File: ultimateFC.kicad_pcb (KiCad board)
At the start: 6 copper layers, 36 x 36 mm, 247 parts, among them J1 Conn_Coaxial, J2 Conn_Coaxial, J3 Conn_Coaxial, J4 Conn_Coaxial, J5 Conn_Coaxial, J6 Conn_Coaxial, J7 USB_B_Micro, SW1 SW_Push, U1 LMR33630CQRNX, U2 TPS62824ADMQ, U3 LMR33620CRNXT, U4 S25FL064L, U5 DPS310, U6 STM32H735VGH6, U7 ICM-20602, U8 BMI270, Y1 CSTNE8M00G550000R0

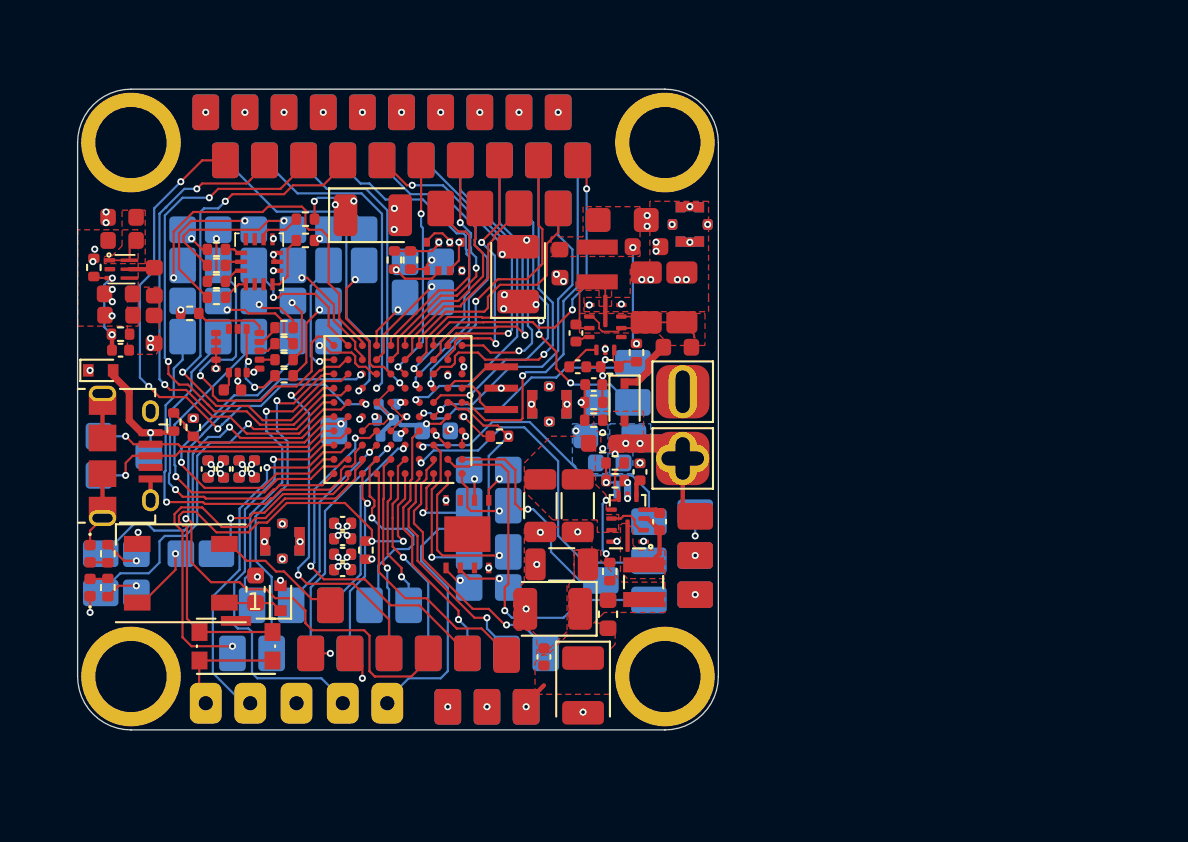
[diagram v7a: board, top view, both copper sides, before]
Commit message: tons of vias
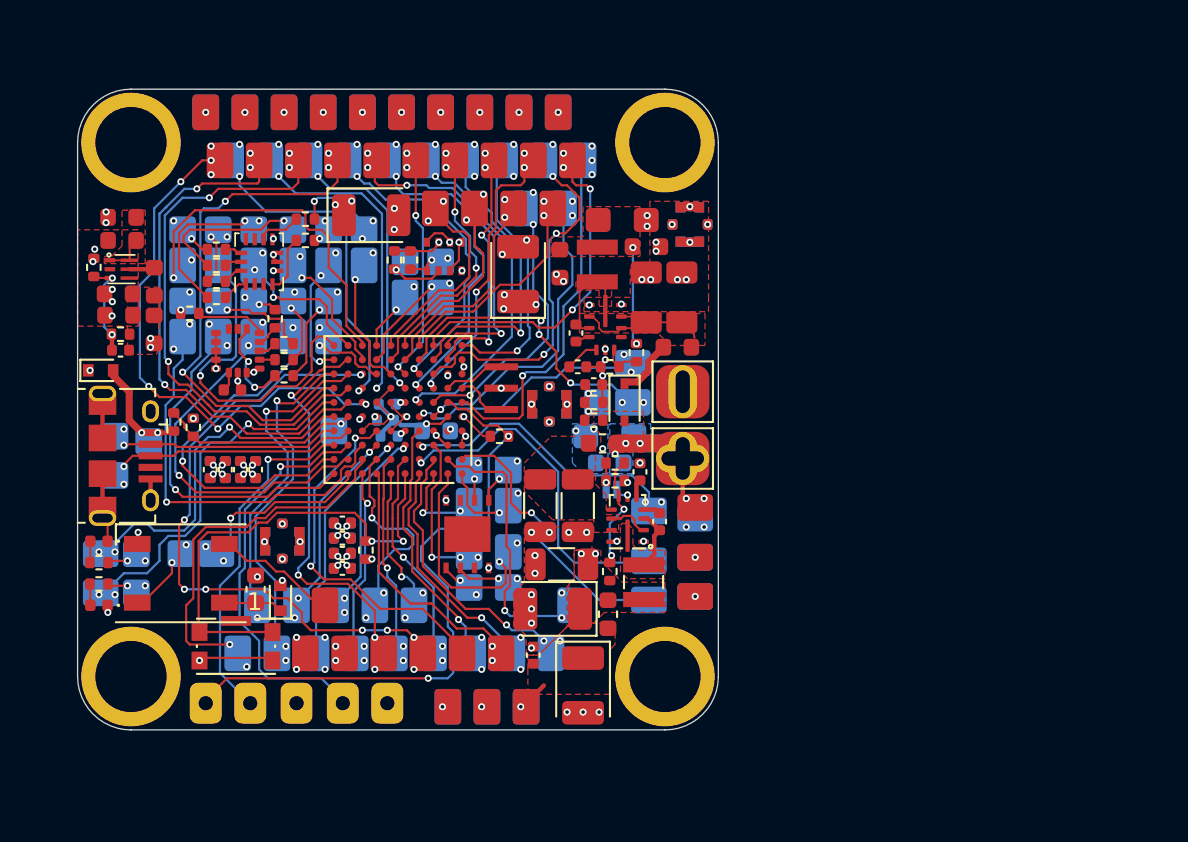
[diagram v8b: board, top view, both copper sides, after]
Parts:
- moved TP25 10.2 mm to (114.4, 131.5)
- moved TP88 10.2 mm to (104.2, 131.5)
- moved TP110 5.20 mm to (106.7, 131.5)
- moved TP111 5.20 mm to (111.9, 131.5)
- moved TP124 4.41 mm to (124.7, 126.0), turned to 180 degrees
- moved TP107 2.92 mm to (129.1, 125.7)
- moved D5 1.12 mm to (98.2, 126.0), turned to 180 degrees
- moved TP136 0.90 mm to (99.1, 116.5)
- moved TP137 0.90 mm to (99.1, 118.7)
- moved D4 0.86 mm to (98.2, 122.4), turned to 180 degrees
- moved TP138 0.80 mm to (101.0, 116.8)
- moved R14 0.71 mm to (108.1, 109.9), turned to -90 degrees
- moved R25 0.71 mm to (98.2, 123.6), turned to 180 degrees
- moved C39 0.61 mm to (122.6, 128.8)
- moved TP114 0.60 mm to (129.1, 120.7)
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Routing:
- net /NRST: track 25.4 -> 36.5 mm, vias 1 -> 2
- net Net-(TP124-Pad1): track 20.3 -> 14.8 mm, vias 1 -> 3
- net Net-(R12-Pad1): track 30.4 -> 26.4 mm
- net SWDIO: track 23.0 -> 19.6 mm
- net +3V3: track 20.3 -> 16.9 mm, vias 24 -> 26
- net MISO_FLASH: track 8.17 -> 11.4 mm, vias 1 -> 2
- net Net-(TP73-Pad1): track 23.3 -> 20.2 mm, vias 1 -> 2
- net Net-(TP107-Pad1): track 12.5 -> 15.6 mm
- net SWDCLK: track 20.7 -> 22.3 mm
- net /MISO_20602: track 2.68 -> 1.02 mm, vias 1 -> 2
- net +5V: track 1.99 -> 0.34 mm, vias 19 -> 20
- net GND: track 18.9 -> 17.5 mm, vias 77 -> 86
- net Net-(TP116-Pad1): track 14.7 -> 16.1 mm, vias 1 -> 3
- net UART3_RX: track 36.5 -> 35.2 mm, vias 2 -> 8
- net Net-(J7-Pad3): track 15.4 -> 14.2 mm, vias 1 -> 2
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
